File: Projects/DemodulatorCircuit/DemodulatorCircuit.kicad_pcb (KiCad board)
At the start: 2 copper layers, 58.4 x 40.6 mm, 22 parts, among them IC2 MC74ACT86DG, J1 SMA-J-P-H-ST-EM1, J2 Conn_01x02, J3 SMA-J-P-H-ST-EM1, U1 TLV3501AID, U2 TLV2374ID, U3 SFECF10M7EA00-R0, U4 SN74ACT04IDREP

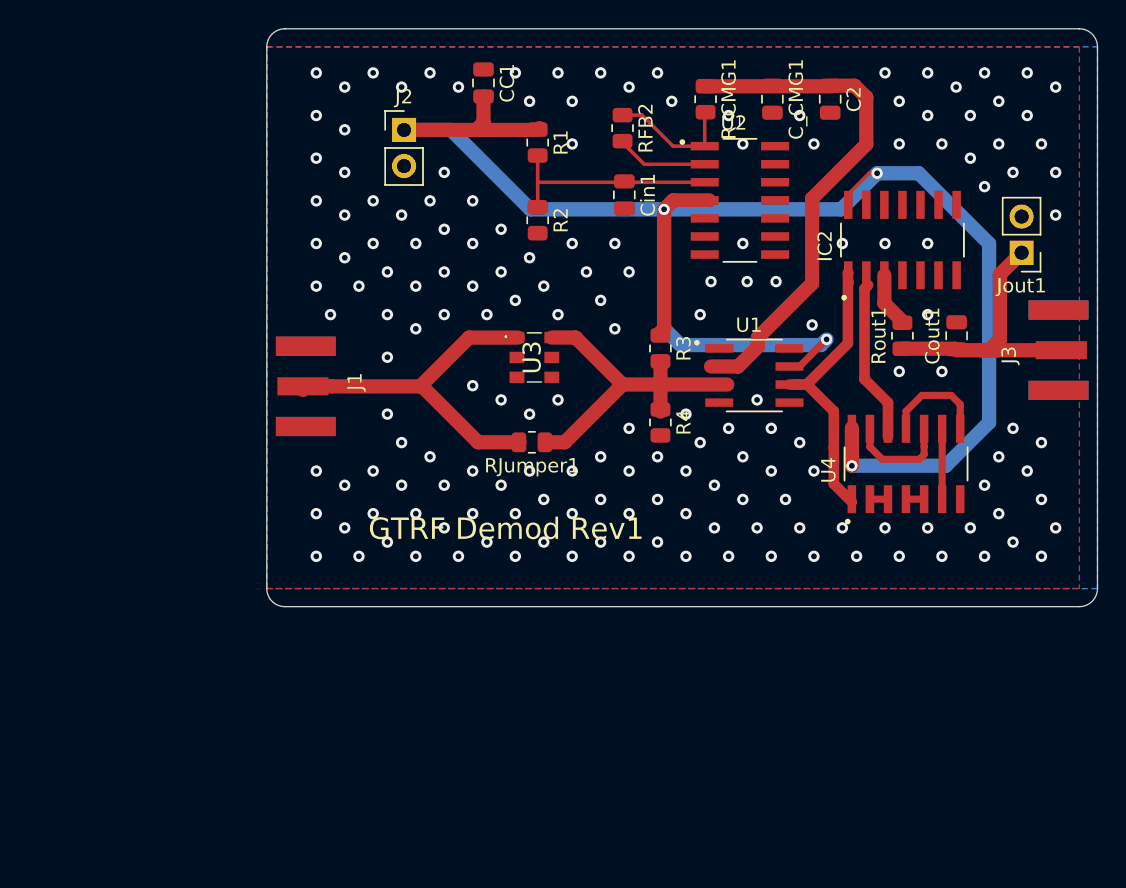
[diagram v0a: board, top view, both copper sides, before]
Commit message: created a balun to single end board
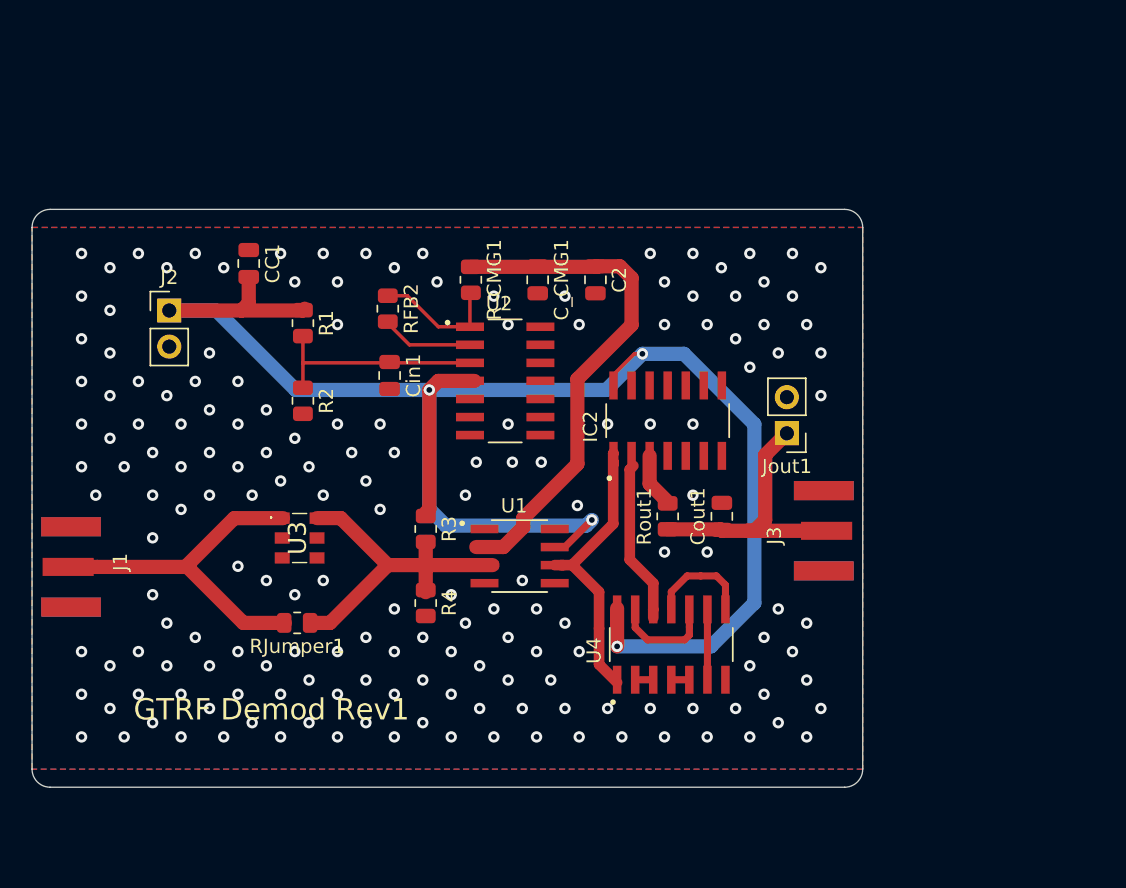
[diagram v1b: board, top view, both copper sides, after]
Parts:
- moved C_CMG1 20.8 mm to (68.6, 30.4)
- moved Cin1 20.8 mm to (58.2, 37.1)
- moved Jout1 20.8 mm to (86.1, 41.1)
- moved R_CMG1 20.8 mm to (63.9, 30.4)
- moved U2 20.8 mm to (66.3, 37.5)
- moved J2 20.8 mm to (42.7, 32.5)
- moved RFB2 20.8 mm to (58.0, 32.4)
- moved U4 20.8 mm to (78.0, 56.0)
- moved J1 20.8 mm to (35.6, 50.5)
- moved R1 20.8 mm to (52.1, 33.4)
- moved R2 20.8 mm to (52.1, 38.9)
- moved U3 20.8 mm to (51.7, 48.5)
- moved C2 20.8 mm to (72.6, 30.4)
- moved CC1 20.8 mm to (48.3, 29.2)
- moved Cout1 20.8 mm to (81.5, 47.0)
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
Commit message: This is the latest version with updated footprints etc
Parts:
- added C_Inv_1: 8.2pF, Capacitor_SMD:C_0603_1608Metric, F.Cu at (72.9, 61.2)
- added C_Inv_2: 8.2pF, Capacitor_SMD:C_0603_1608Metric, F.Cu at (78.0, 61.2)
- added C_Inv_3: 8.2pF, Capacitor_SMD:C_0603_1608Metric, F.Cu at (84.3, 57.0)
- added C_Inv_4: 8.2pF, Capacitor_SMD:C_0603_1608Metric, F.Cu at (82.3, 51.4)
- added C_Inv_5: 8.2pF, Capacitor_SMD:C_0603_1608Metric, B.Cu at (79.8, 48.0)
- added R_Inv_1: 1k, Resistor_SMD:R_0603_1608Metric, F.Cu at (74.4, 62.9)
- added R_Inv_2: 1k, Resistor_SMD:R_0603_1608Metric, F.Cu at (79.6, 63.1)
- added R_Inv_3: 1k, Resistor_SMD:R_0603_1608Metric, F.Cu at (86.3, 55.3)
- added R_Inv_4: 1k, Resistor_SMD:R_0603_1608Metric, F.Cu at (79.2, 49.8)
- added R_Inv_5: 1k, Resistor_SMD:R_0603_1608Metric, B.Cu at (76.8, 48.8)
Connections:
- U4 pad 11: /4Y -> Net-(R_Inv_4-Pad2)
- U4 pad 13: /5Y -> Net-(R_Inv_5-Pad2)
- U4 pad 3: /1Y -> Net-(R_Inv_1-Pad2)
- U4 pad 5: /2Y -> Net-(R_Inv_2-Pad2)
- U4 pad 9: /3Y -> Net-(R_Inv_3-Pad2)
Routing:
- net Net-(R_Inv_3-Pad2): track 0.00 -> 7.76 mm
- net Net-(R_Inv_5-Pad2): track 0.00 -> 6.11 mm, vias 0 -> 1
- net Net-(R_Inv_1-Pad2): track 0.00 -> 5.71 mm
- net Net-(R_Inv_2-Pad2): track 0.00 -> 5.55 mm
- net Net-(R_Inv_4-Pad2): track 0.00 -> 4.15 mm
- net /1Y: track 1.29 -> 5.25 mm
- net /4Y: track 8.34 -> 4.39 mm
- net /2Y: track 1.30 -> 5.04 mm
- net /3Y: track 5.14 -> 7.54 mm
- net /5Y: track 8.00 -> 7.08 mm, vias 0 -> 1
- net GND: vias 175 -> 148

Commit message: post board review they are all ready to order
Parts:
- C_Inv_5, R_Inv_5: moved to F.Cu
- moved R_Inv_5 13.7 mm to (86.4, 58.6), turned to 90 degrees
- moved C_Inv_5 13.0 mm to (84.3, 60.2), turned to 270 degrees
- moved C_Inv_4 7.75 mm to (74.9, 53.8), turned to 180 degrees
- moved R_Inv_3 6.10 mm to (81.3, 51.8), turned to 0 degrees
- moved C_Inv_3 5.69 mm to (79.6, 53.7), turned to 180 degrees
- moved R_Inv_4 3.21 mm to (76.7, 51.8), turned to 0 degrees
- moved R_Inv_1 2.99 mm to (74.3, 65.8)
- moved U4 2.99 mm to (77.9, 59.0)
- moved R_Inv_2 2.99 mm to (79.5, 66.1)
- moved C_Inv_1 2.99 mm to (72.8, 64.2)
- moved C_Inv_2 2.99 mm to (77.9, 64.2)
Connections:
- C_Inv_3 pad 1: /3Y -> /5Y
- C_Inv_4 pad 1: /4Y -> /6Y
- C_Inv_5 pad 1: /5Y -> /3Y
- IC2 pad 2: /IFQ_LIM -> /4Y
- R_Inv_3 pad 1: /3Y -> /5Y
- R_Inv_4 pad 1: /4Y -> /6Y
- R_Inv_5 pad 1: /5Y -> /3Y
- U4 pad 12: /IFQ_LIM -> /6Y
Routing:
- net /4Y: track 4.39 -> 23.5 mm
- net /IFQ_LIM: track 11.5 -> 0.00 mm
- net Net-(R_Inv_5-Pad2): track 6.11 -> 13.5 mm, vias 1 -> 0
- net /6Y: track 0.00 -> 5.11 mm
- net +5V: track 124.6 -> 127.6 mm
- net /IF_Lim: track 20.2 -> 22.8 mm
- net Net-(R_Inv_3-Pad2): track 7.76 -> 5.69 mm
- net /5Y: track 7.08 -> 5.41 mm, vias 1 -> 0
- net Net-(R_Inv_4-Pad2): track 4.15 -> 5.21 mm
- net /3Y: track 7.54 -> 8.11 mm
- net GND: vias 148 -> 177
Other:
- board size 58.4 x 40.6 mm -> 58.6 x 45.7 mm
